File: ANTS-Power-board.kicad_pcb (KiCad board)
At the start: 2 copper layers, 80 x 80 mm, 32 parts, among them J1 DF11-12DP, J2 DF11-12DP, J3 Phoenix 1751248, J4 Phoenix 1751248, U1 TPS62916RPYR, U2 LP2985-3.3

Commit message: Add LDO schematic + layout
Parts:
- added C17: 1u, Capacitor_SMD:C_0603_1608Metric, F.Cu at (136.8, 129.4)
- added C18: 10n, Capacitor_SMD:C_0402_1005Metric, F.Cu at (140.5, 132.5)
- added C19: 4.7u, Capacitor_SMD:C_0603_1608Metric, F.Cu at (142.8, 129.4)
- added R5: 0, Resistor_SMD:R_0603_1608Metric, F.Cu at (136.0, 132.4)
- added TP1: LDO_IN, TestPoint:TestPoint_THTPad_D1.0mm_Drill0.5mm, F.Cu at (135.0, 125.6)
- added TP2: ON/OFF, TestPoint:TestPoint_THTPad_D1.0mm_Drill0.5mm, F.Cu at (136.8, 134.8)
- moved U2 10.0 mm to (139.9, 130.1)
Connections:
- U2 pad 1: unconnected-(U2-VIN-Pad1) -> VBAT+
- U2 pad 2: unconnected-(U2-GND-Pad2) -> VBAT-
- U2 pad 3: unconnected-(U2-ON/~{OFF}-Pad3) -> /3.3v_LDO/ON/~{OFF}
- U2 pad 4: unconnected-(U2-BP-Pad4) -> /3.3v_LDO/BP
- U2 pad 5: unconnected-(U2-VOUT-Pad5) -> 3V3_OUTPUT
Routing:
- net VBAT+: track 8.85 -> 15.4 mm, vias 0 -> 2
- net /3.3v_LDO/ON/~{OFF}: track 0.00 -> 4.89 mm
- net /3.3v_LDO/BP: track 0.00 -> 1.51 mm
- added copper zone on F.Cu, net 3V3_OUTPUT

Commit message: Finished schematic & layout
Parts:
- removed C13, C14: 22uF, Capacitor_SMD:C_1206_3216Metric
- removed R2: 10k, Resistor_SMD:R_0402_1005Metric
- C1, C2: footprint Capacitor_SMD:C_1210_3225Metric -> Capacitor_SMD:C_0805_2012Metric
- C10, C11, C12, C15, C16, C7, C8, C9: footprint Capacitor_SMD:C_1206_3216Metric -> Capacitor_SMD:C_0805_2012Metric
- C3, C4, C6: footprint Capacitor_SMD:C_0603_1608Metric -> Capacitor_SMD:C_0402_1005Metric
- C5: footprint Capacitor_SMD:C_1206_3216Metric -> Capacitor_SMD:C_0402_1005Metric
- FB1: value FerriteBead -> BLE32SN120SN1L
- moved J3 10.3 mm to (168.2, 90.0)
- moved C15 5.05 mm to (159.2, 89.3)
- moved C16 5.05 mm to (161.7, 89.3)
- moved FB1 4.90 mm to (152.9, 91.9), turned to 0 degrees
- moved R1 4.59 mm to (116.2, 92.8), turned to 180 degrees
- moved R4 3.09 mm to (117.0, 90.8), turned to 90 degrees
- moved C18 2.90 mm to (142.6, 130.5), turned to 90 degrees
- moved J4 2.90 mm to (168.2, 125.8)
- moved R3 1.83 mm to (115.8, 90.8), turned to -90 degrees
- moved C5 1.79 mm to (120.2, 89.0)
- moved C19 1.44 mm to (144.0, 128.6), turned to 0 degrees
- moved C1 1.08 mm to (122.4, 87.0)
- moved C2 1.02 mm to (122.4, 96.5)
- moved C6 0.90 mm to (118.2, 90.8), turned to 90 degrees
- moved C11 0.86 mm to (139.2, 89.3)
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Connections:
- FB1 pad 1: 5V_OUTPUT -> /5V SMPS/VO
- FB1 pad 2: /5V SMPS/VO -> 5V_OUTPUT
- L1 pad 1: /5V SMPS/VO -> /5V SMPS/SW
- L1 pad 2: /5V SMPS/SW -> /5V SMPS/VO
- U1 pad 5: /5V SMPS/PG -> unconnected-(U1-PG-Pad5)
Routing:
- net VBAT-: track 0.00 -> 10.7 mm, vias 48 -> 46
- net VBAT+: track 15.4 -> 24.5 mm, vias 2 -> 4
- net /5V SMPS/VO: track 26.6 -> 17.6 mm
- net 5V_OUTPUT: track 61.9 -> 54.3 mm
- net /5V SMPS/S-CONF: track 1.09 -> 4.68 mm
- net /5V SMPS/BOOT: track 5.20 -> 2.01 mm
- net /5V SMPS/SW: track 6.55 -> 4.03 mm
- net /5V SMPS/PG: track 2.02 -> 0.00 mm
- net /5V SMPS/NR/SS: track 2.52 -> 1.62 mm
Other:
- board text added: "+ 3V3 -"
- board text added: "+ 5V -"
- board text removed: "3V3"
- board text removed: "5V"

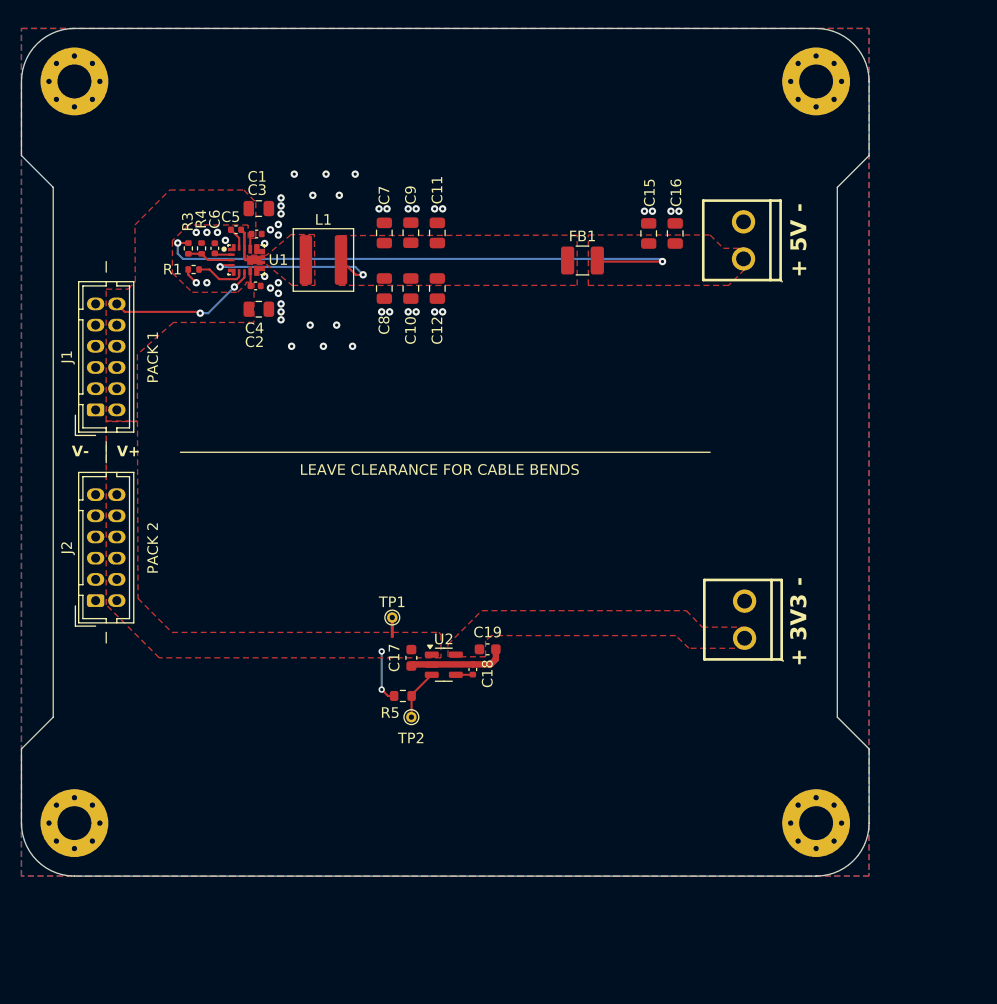
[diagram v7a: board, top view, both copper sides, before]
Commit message: rewire LDO input to 5V from VBAT and verify DRC
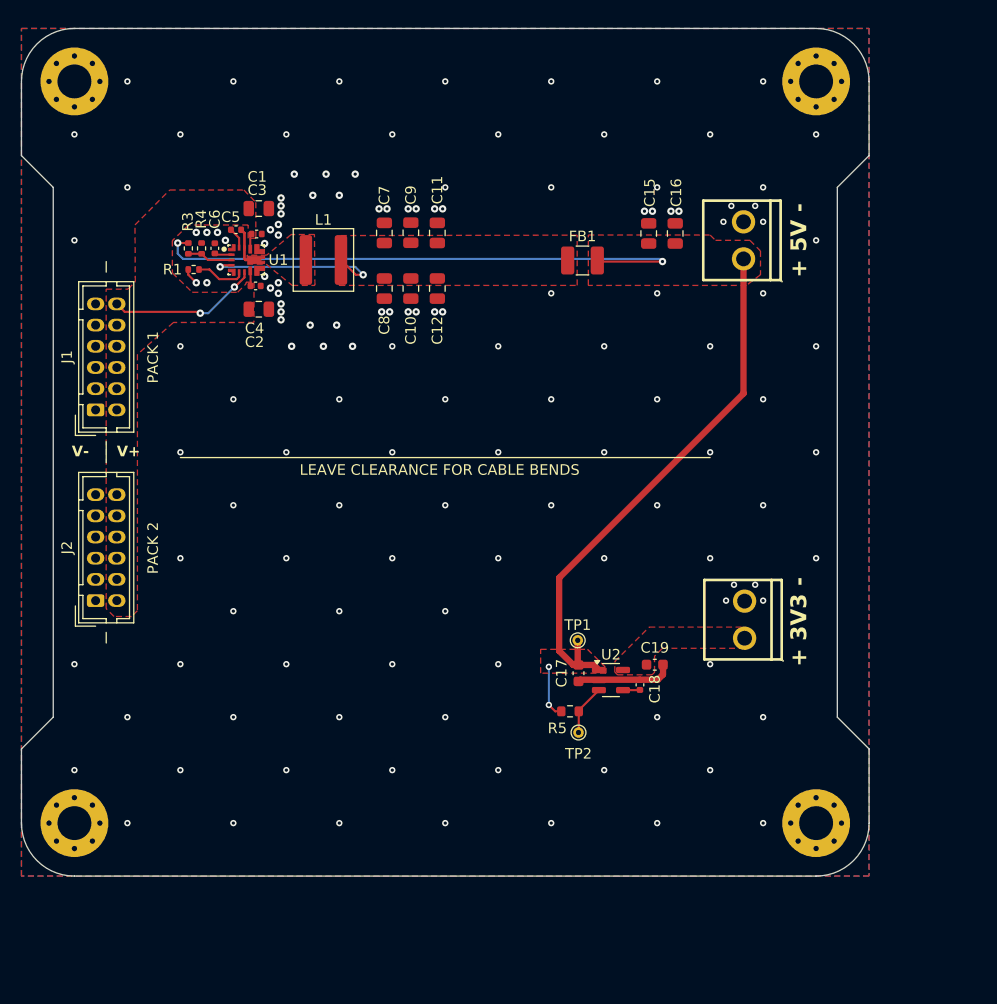
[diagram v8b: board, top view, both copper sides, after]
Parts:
- moved TP1 17.6 mm to (152.5, 127.8)
- moved C19 15.8 mm to (159.8, 130.1)
- moved C18 15.8 mm to (158.4, 131.9)
- moved R5 15.8 mm to (151.8, 134.4)
- moved C17 15.8 mm to (152.6, 130.8)
- moved TP2 15.8 mm to (152.6, 136.4)
- moved U2 15.8 mm to (155.6, 131.5)
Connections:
- C17 pad 1: VBAT+ -> 5V_OUTPUT
- R5 pad 2: VBAT+ -> 5V_OUTPUT
- TP1 pad 1: VBAT+ -> 5V_OUTPUT
- U2 pad 1: VBAT+ -> 5V_OUTPUT
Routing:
- net 5V_OUTPUT: track 54.3 -> 110.3 mm, vias 2 -> 4
- net VBAT+: track 24.5 -> 17.7 mm, vias 4 -> 2
- net VBAT-: vias 46 -> 140
